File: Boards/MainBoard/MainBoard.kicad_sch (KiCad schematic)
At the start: 18 parts, among them J1 Conn_02x08_Counter_Clockwise, J11 Conn_02x10_Counter_Clockwise, J12 Conn_02x10_Counter_Clockwise, J13 Conn_02x10_Counter_Clockwise, J14 Conn_02x10_Counter_Clockwise, J2 Conn_02x08_Counter_Clockwise, J3 Conn_02x08_Counter_Clockwise, J4 TBP01R1-508-06BE, J5 Conn_02x10_Counter_Clockwise, J6 TBP01R1-508-06BE, J7 TBP02R2W-381-08BE, J8 TBP02R2W-381-08BE

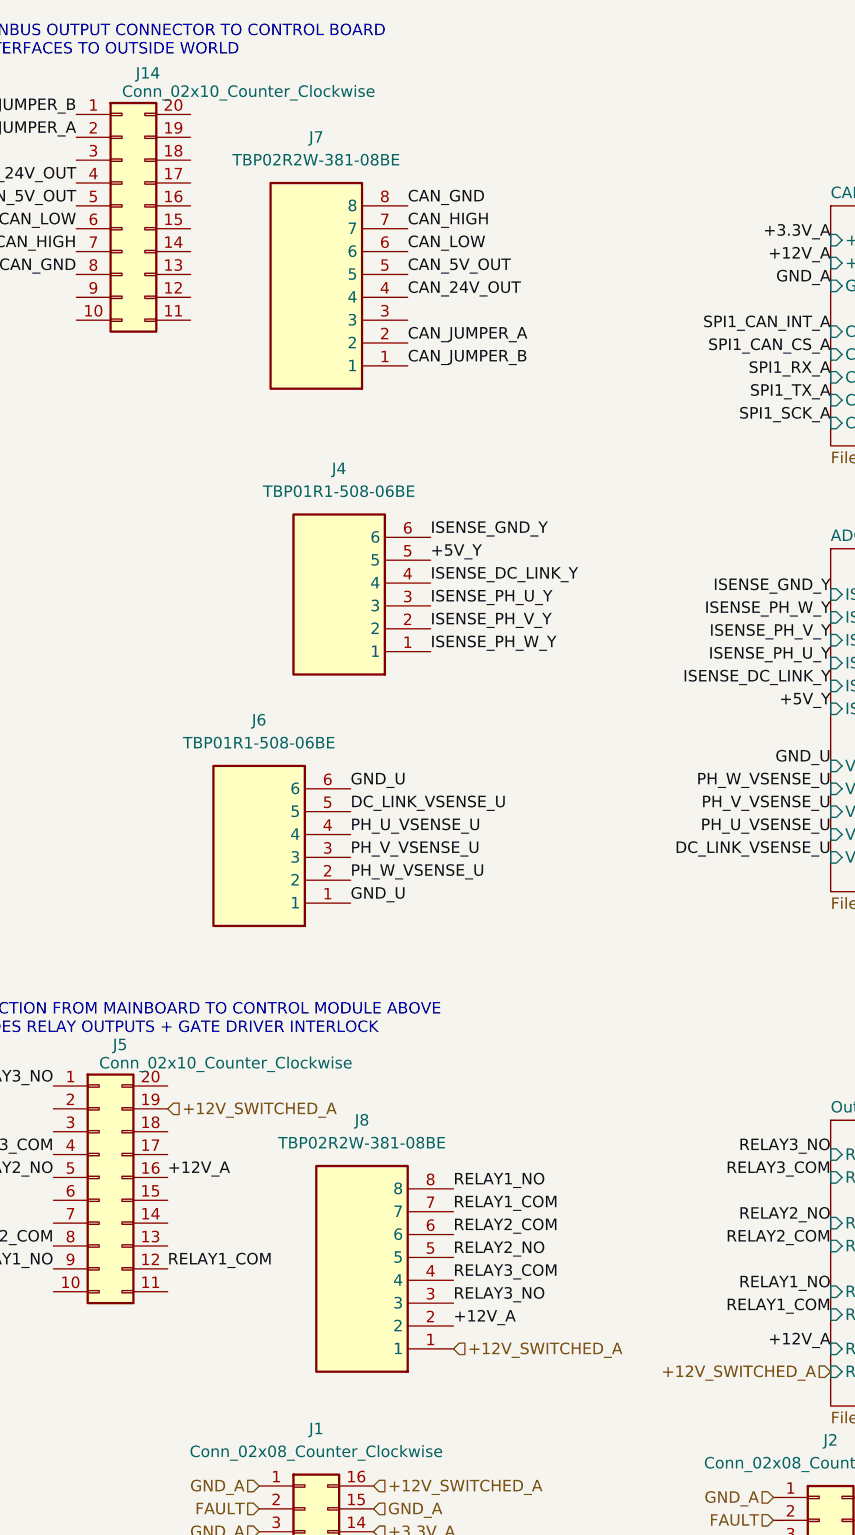
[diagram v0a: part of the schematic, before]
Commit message: layout control boards, add baseplate, refine mechanical layout
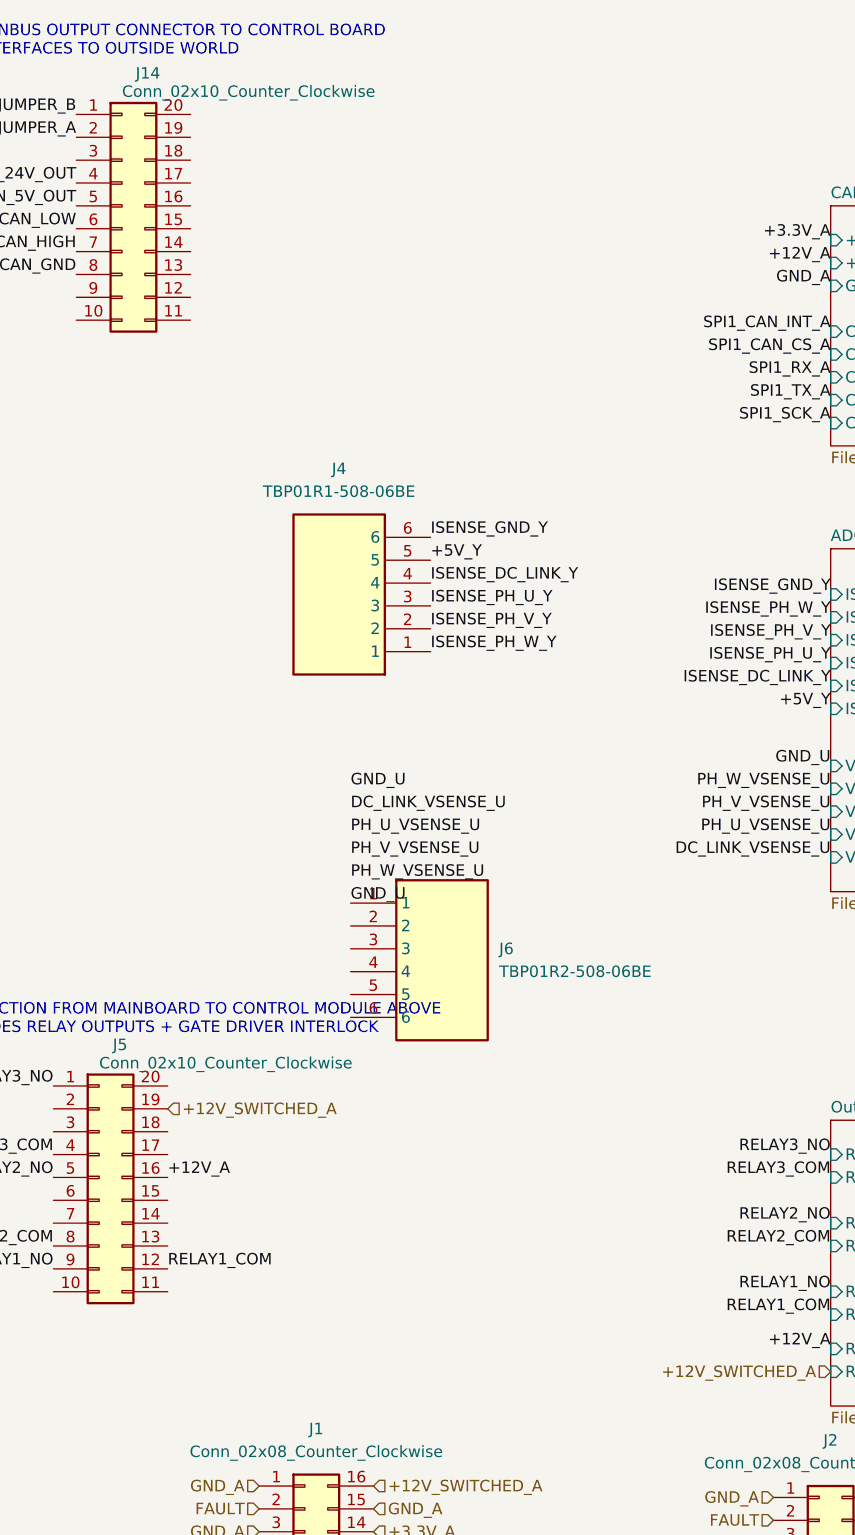
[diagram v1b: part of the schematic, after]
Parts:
- removed J6: TBP01R1-508-06BE, InverterCom:TBP01R150806BE, symbol InverterCom:TBP01R1-508-06BE
- removed J7, J8: TBP02R2W-381-08BE, InverterCom:TBP02R2W38108BE, symbol InverterCom:TBP02R2W-381-08BE
- added J6: TBP01R2-508-06BE, TBP01R250806BE, symbol InverterCom:TBP01R2-508-06BE
- J11, J12, J13, J14, J5: footprint Connector_PinSocket_2.54mm:PinSocket_2x10_P2.54mm_Vertical -> Connector_PinHeader_2.54mm:PinHeader_2x10_P2.54mm_Vertical
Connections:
- net GND_U: now also J6.1

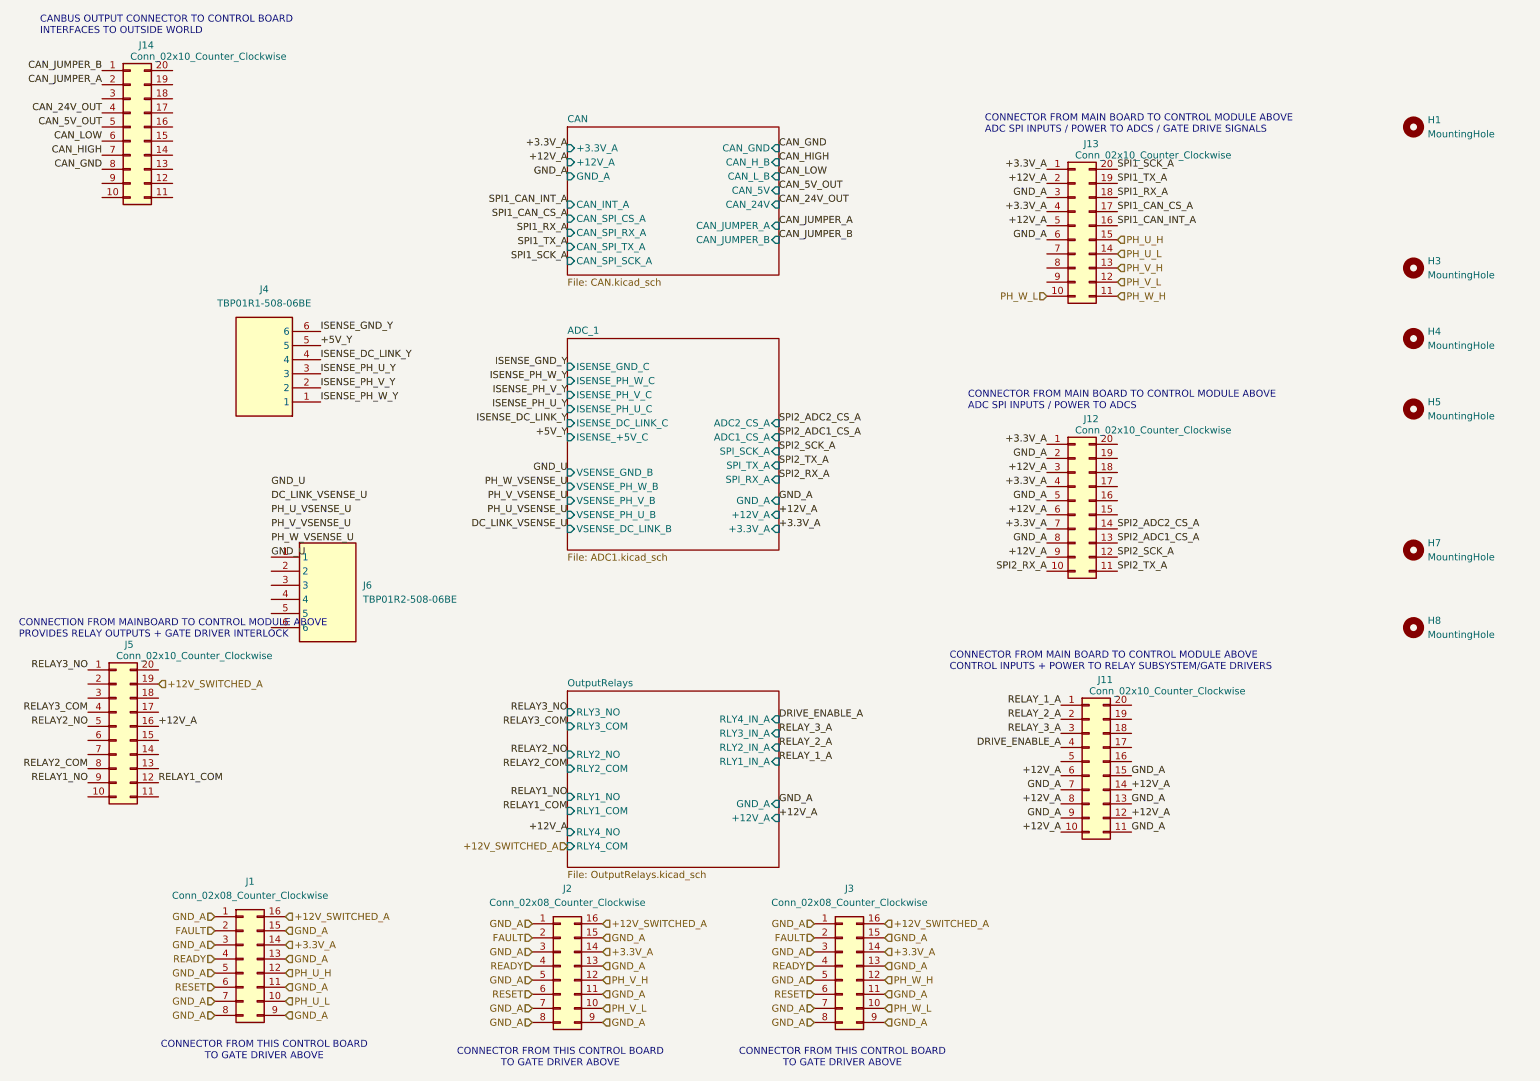
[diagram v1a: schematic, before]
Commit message: Layout mainboard, add EMI filter caps
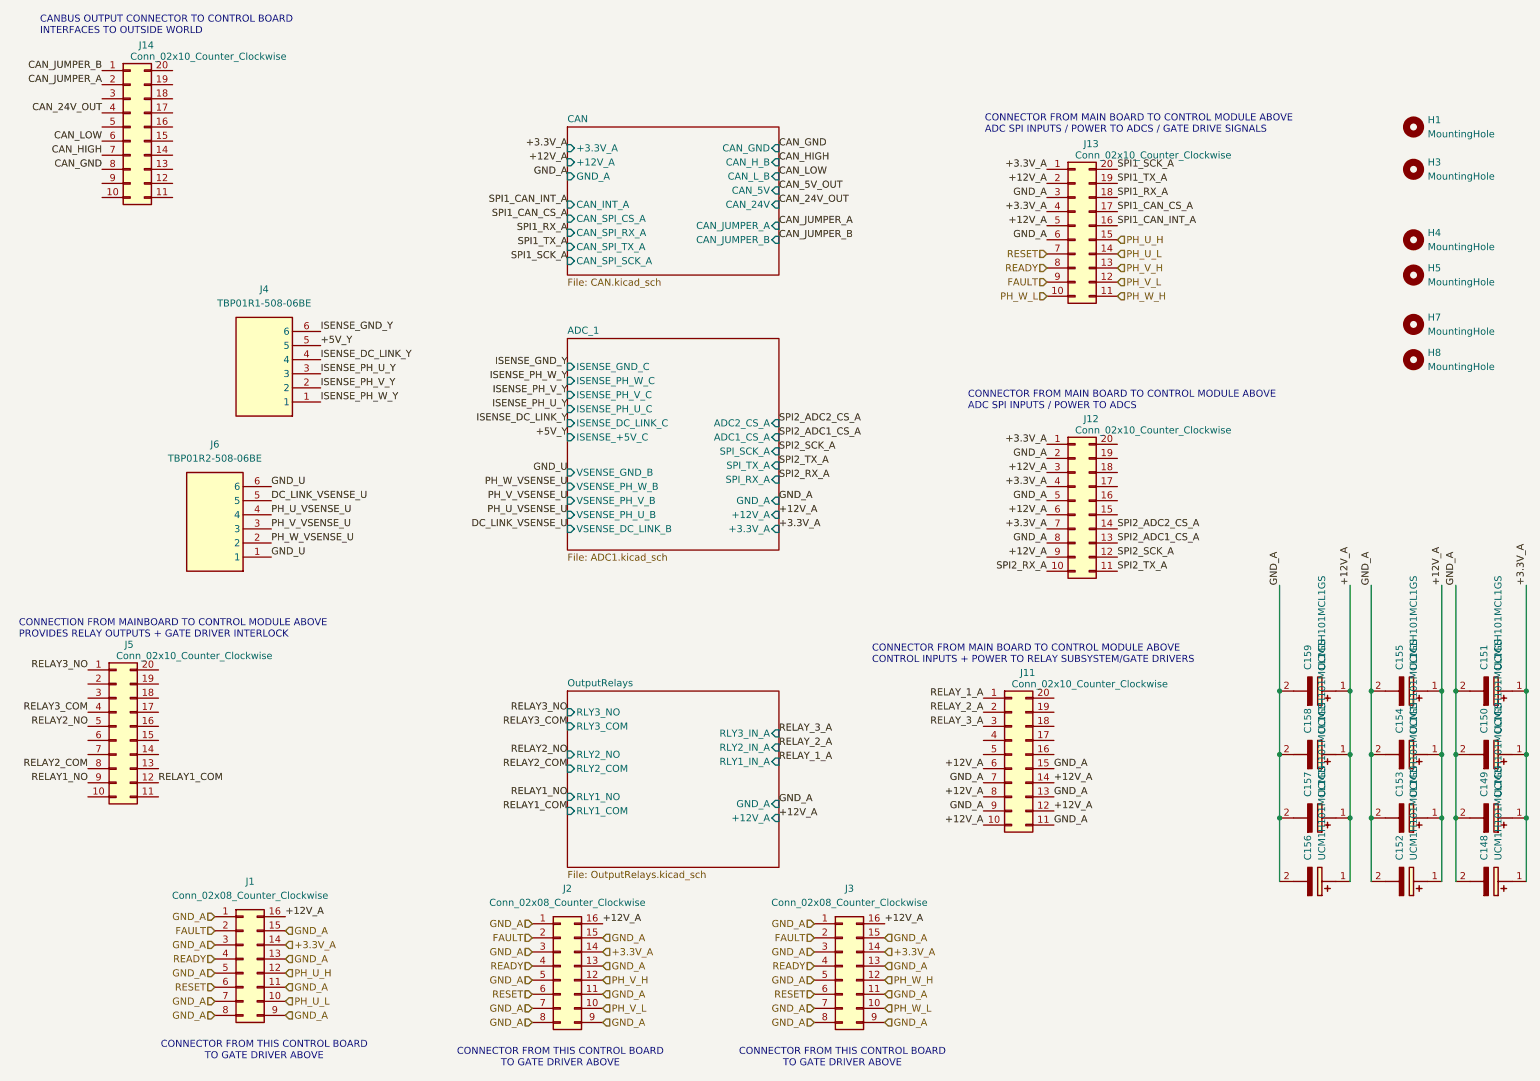
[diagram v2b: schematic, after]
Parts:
- added C148, C149, C150, C151, C152, C153, C154, C155, C156, C157, C158, C159: UCM1H101MCL1GS, InverterCom:CAPAE660X800N, symbol InverterCom:UCM1H101MCL1GS
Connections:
- net +12V_A: now also J1.16 (Pin_16), J2.16 (Pin_16), J3.16 (Pin_16), C152.1 (+), C153.1 (+), C154.1 (+), C155.1 (+), C156.1 (+), C157.1 (+), C158.1 (+), C159.1 (+); no longer J5.16 (Pin_16)
- net +3.3V_A: now also C148.1 (+), C149.1 (+), C150.1 (+), C151.1 (+)
- net CAN_5V_OUT: no longer J14.5 (Pin_5)
- net DC_LINK_VSENSE_U: now also J6.5
- net FAULT: now also J13.9 (Pin_9)
- net GND_A: now also C148.2 (-), C149.2 (-), C150.2 (-), C151.2 (-), C152.2 (-), C153.2 (-), C154.2 (-), C155.2 (-), C156.2 (-), C157.2 (-), C158.2 (-), C159.2 (-)
- net GND_U: now also J6.6
- net PH_U_VSENSE_U: now also J6.4
- net PH_V_VSENSE_U: now also J6.3
- net PH_W_VSENSE_U: now also J6.2
- net READY: now also J13.8 (Pin_8)
- net RESET: now also J13.7 (Pin_7)
- removed net +12V_SWITCHED_A: J1.16 (Pin_16), J2.16 (Pin_16), J3.16 (Pin_16), J5.19 (Pin_19)
- net DRIVE_ENABLE_A: no longer names the net of J11.4 (Pin_4)
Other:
- sheet OutputRelays ports: added none; removed RLY4_COM, RLY4_IN_A, RLY4_NO
- moved on the sheet: H3, H4, H5, H7, H8, J11, J6
